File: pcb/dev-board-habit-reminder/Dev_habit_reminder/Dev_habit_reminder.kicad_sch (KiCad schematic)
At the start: 10 parts, among them J1 I2C BREAKOUT, SW1 SW_Push, SW2 SW_Push, SW3 SW_Push, U1 ESP32-DevKitC

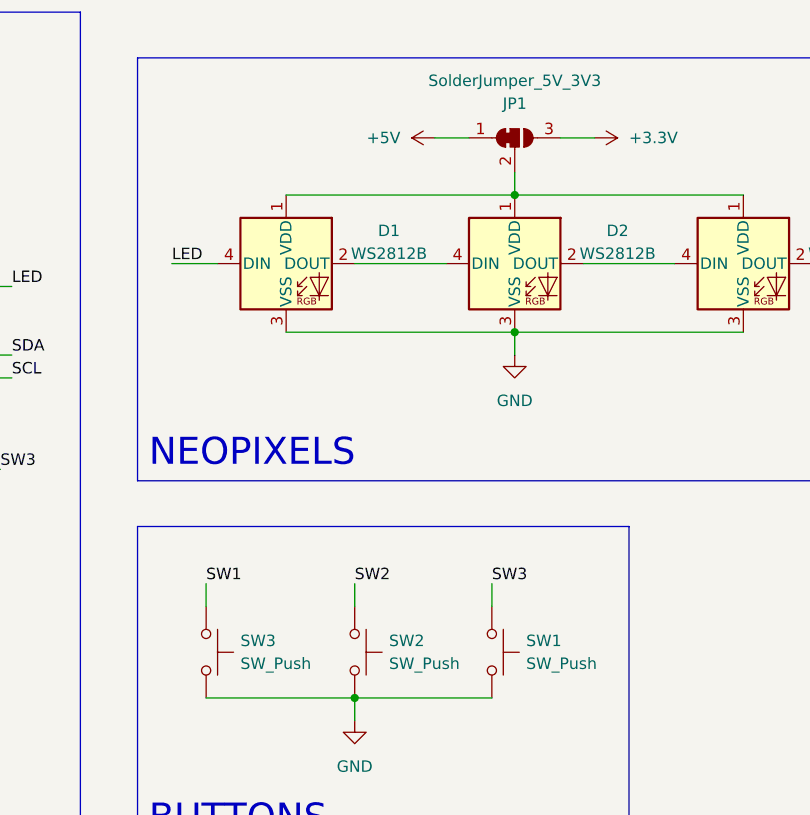
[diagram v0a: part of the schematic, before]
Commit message: PCB Track width definition, rerouting
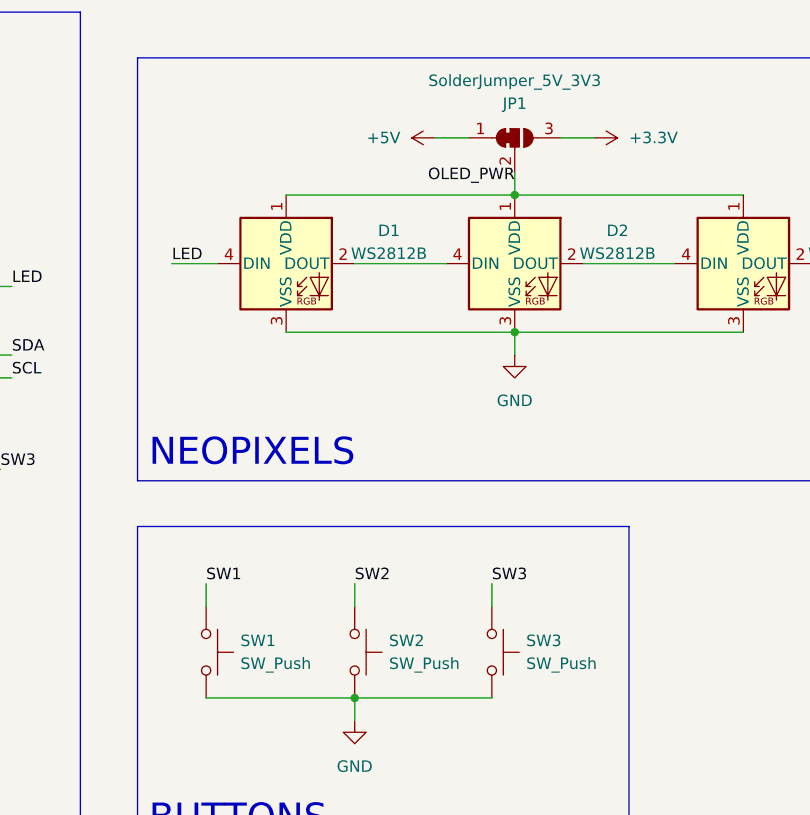
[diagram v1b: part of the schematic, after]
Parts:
- renumbered SW3 to SW1, SW1 to SW3
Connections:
- net OLED_PWR: now reaches D1.1 (VDD), D2.1 (VDD), D3.1 (VDD), JP1.2 (C)
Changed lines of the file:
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@@
     (effects (font (size 1.27 1.27)) (justify left bottom))
+  )
+  (label "OLED_PWR" (at 224.79 59.69 180) (fields_autoplaced)
+    (effects (font (size 1.27 1.27)) (justify right bottom))
   )
   (label "SW2" (at 207.01 104.14 0) (fields_autoplaced)
@@
   (label "SCL" (at 168.91 81.28 0) (fields_autoplaced)
     (effects (font (size 1.27 1.27)) (justify left bottom))
+  )
+  (netclass_flag "" (length 2.54) (shape round) (at 234.95 68.58 180) (fields_autoplaced)
+    (effects (font (size 1.27 1.27)) (justify right bottom))
+    (property "Netclass" "Signal" (at 235.6485 71.12 0)
+      (effects (font (size 1.27 1.27) italic) (justify left) hide)
+    )
+  )
+  (netclass_flag "" (length 2.54) (shape round) (at 210.82 68.58 180) (fields_autoplaced)
+    (effects (font (size 1.27 1.27)) (justify right bottom))
+    (property "Netclass" "Signal" (at 211.5185 71.12 0)
+      (effects (font (size 1.27 1.27) italic) (justify left) hide)
+    )
   )
   (symbol (lib_id "power:GND") (at 60.96 125.73 270) (unit 1)
@@
   (symbol (lib_id "Switch:SW_Push") (at 190.5 111.76 270) (unit 1)
     (in_bom yes) (on_board yes) (dnp no) (fields_autoplaced)
-    (property "Reference" "SW3" (at 194.31 110.49 90)
+    (property "Reference" "SW1" (at 194.31 110.49 90)
       (effects (font (size 1.27 1.27)) (justify left))
     )
@@
       (project "Dev_habit_reminder"
         (path "/00a14bb3-c2ab-4ff5-bcca-f0dba2d9bd5e"
-          (reference "SW3") (unit 1)
+          (reference "SW1") (unit 1)
         )
       )
@@
   (symbol (lib_id "Switch:SW_Push") (at 222.25 111.76 270) (unit 1)
     (in_bom yes) (on_board yes) (dnp no) (fields_autoplaced)
-    (property "Reference" "SW1" (at 226.06 110.49 90)
+    (property "Reference" "SW3" (at 226.06 110.49 90)
       (effects (font (size 1.27 1.27)) (justify left))
     )
@@
       (project "Dev_habit_reminder"
         (path "/00a14bb3-c2ab-4ff5-bcca-f0dba2d9bd5e"
-          (reference "SW1") (unit 1)
+          (reference "SW3") (unit 1)
         )
       )

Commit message: Board re-routing
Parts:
- D1, D3: MPN (none) -> C2843785
- SW1, SW2, SW3: MPN (none) -> C410366
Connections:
- net OLED_PWR renamed NEOPIXEL_PWR
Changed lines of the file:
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@@
     (effects (font (size 1.27 1.27)) (justify left bottom))
   )
-  (label "OLED_PWR" (at 224.79 59.69 180) (fields_autoplaced)
+  (label "NEOPIXEL_PWR" (at 224.79 59.69 180) (fields_autoplaced)
     (effects (font (size 1.27 1.27)) (justify right bottom))
   )
@@
       (effects (font (size 1.27 1.27)) hide)
     )
+    (property "MPN" "C410366" (at 190.5 111.76 90)
+      (effects (font (size 1.27 1.27)) hide)
+    )
     (pin "1")
     (pin "2")
@@
     )
     (property "Datasheet" "~" (at 227.33 111.76 0)
+      (effects (font (size 1.27 1.27)) hide)
+    )
+    (property "MPN" "C410366" (at 222.25 111.76 90)
       (effects (font (size 1.27 1.27)) hide)
     )
@@
     (property "Datasheet" "https://cdn-shop.adafruit.com/datasheets/WS2812B.pdf" (at 252.73 78.105 0)
       (effects (font (size 1.27 1.27)) (justify left top) hide)
+    )
+    (property "MPN" "C2843785" (at 250.19 68.58 0)
+      (effects (font (size 1.27 1.27)) hide)
     )
     (pin "1")
@@
       (effects (font (size 1.27 1.27)) hide)
     )
+    (property "MPN" "C410366" (at 207.01 111.76 90)
+      (effects (font (size 1.27 1.27)) hide)
+    )
     (pin "1")
     (pin "2")
@@
     )
   )
-  (symbol (lib_id "LED:WS2812B") (at 199.39 68.58 0) (unit 1)
+  (symbol (lib_name "WS2812B_1") (lib_id "LED:WS2812B") (at 199.39 68.58 0) (unit 1)
     (in_bom yes) (on_board yes) (dnp no) (fields_autoplaced)
     (property "Reference" "D1" (at 210.82 64.9321 0)
@@
       (effects (font (size 1.27 1.27)) (justify left top) hide)
     )
-    (pin "1")
+    (property "MPN" "C2843785" (at 199.39 68.58 0)
+      (effects (font (size 1.27 1.27)) hide)
+    )
+    (pin "1")

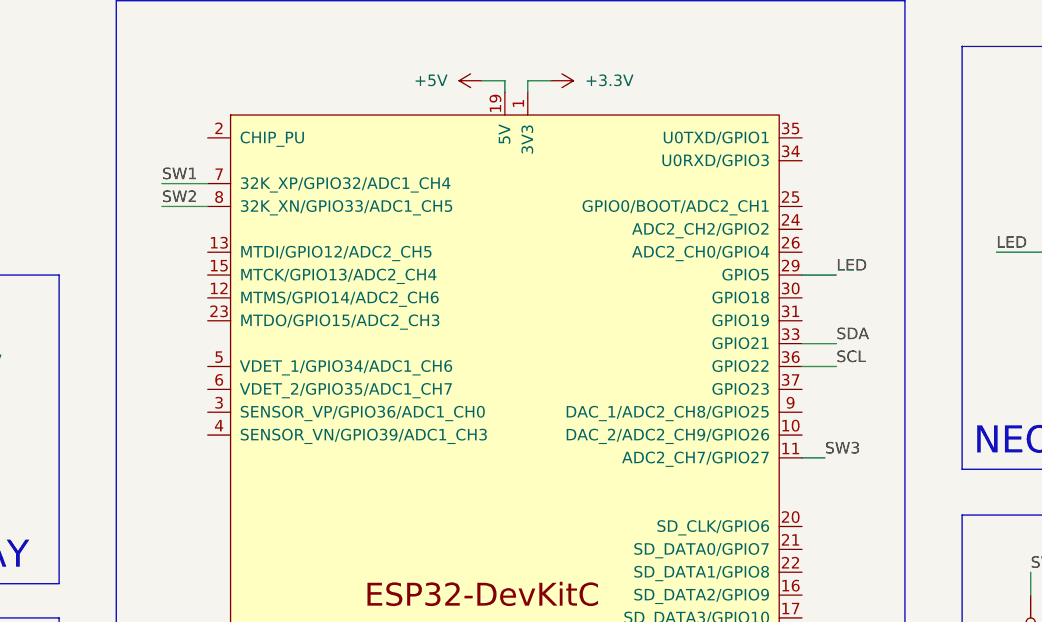
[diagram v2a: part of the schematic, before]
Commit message: Changed button pins for efficient routing
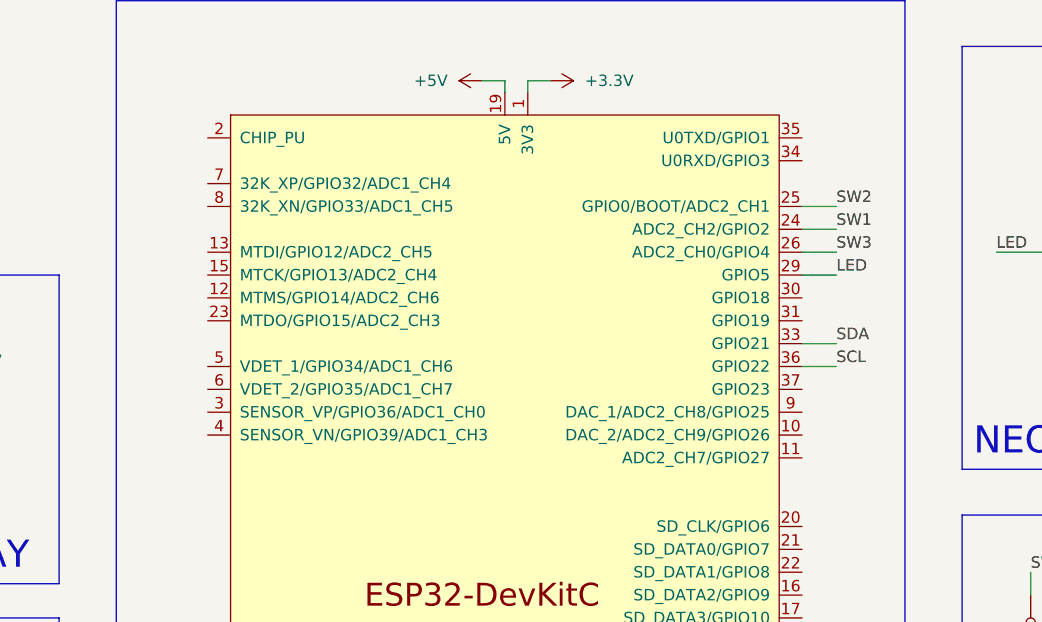
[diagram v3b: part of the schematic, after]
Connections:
- net SW1: now also U1.24 (ADC2_CH2/GPIO2); no longer U1.7 (32K_XP/GPIO32/ADC1_CH4)
- net SW2: now also U1.25 (GPIO0/BOOT/ADC2_CH1); no longer U1.8 (32K_XN/GPIO33/ADC1_CH5)
- net SW3: now also U1.26 (ADC2_CH0/GPIO4); no longer U1.11 (ADC2_CH7/GPIO27)
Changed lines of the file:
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@@
-    (stroke (width 0) (type default))
-  )
-  (wire (pts (xy 93.98 60.96) (xy 99.06 60.96))
     (stroke (width 0) (type default))
   )
@@
   )
   (wire (pts (xy 224.79 76.2) (xy 224.79 78.74))
+    (stroke (width 0) (type default))
+  )
+  (wire (pts (xy 165.1 66.04) (xy 168.91 66.04))
     (stroke (width 0) (type default))
   )
@@
   )
   (wire (pts (xy 233.68 54.61) (xy 229.87 54.61))
+    (stroke (width 0) (type default))
+  )
+  (wire (pts (xy 165.1 63.5) (xy 168.91 63.5))
     (stroke (width 0) (type default))
   )
@@
     (stroke (width 0) (type default))
   )
+  (wire (pts (xy 165.1 68.58) (xy 168.91 68.58))
+    (stroke (width 0) (type default))
+  )
   (wire (pts (xy 60.96 123.19) (xy 60.96 125.73))
     (stroke (width 0) (type default))
@@
     (stroke (width 0) (type default))
   )
-  (wire (pts (xy 93.98 63.5) (xy 99.06 63.5))
-    (stroke (width 0) (type default))
-  )
   (wire (pts (xy 207.01 104.14) (xy 207.01 106.68))
-    (stroke (width 0) (type default))
-  )
-  (wire (pts (xy 165.1 91.44) (xy 167.64 91.44))
     (stroke (width 0) (type default))
   )
@@
     (effects (font (size 1.27 1.27)) (justify left bottom))
   )
-  (label "SW2" (at 93.98 63.5 0) (fields_autoplaced)
-    (effects (font (size 1.27 1.27)) (justify left bottom))
-  )
   (label "SW3" (at 222.25 104.14 0) (fields_autoplaced)
     (effects (font (size 1.27 1.27)) (justify left bottom))
@@
     (effects (font (size 1.27 1.27)) (justify left bottom))
   )
+  (label "SW3" (at 168.91 68.58 0) (fields_autoplaced)
+    (effects (font (size 1.27 1.27)) (justify left bottom))
+  )
   (label "SW1" (at 190.5 104.14 0) (fields_autoplaced)
     (effects (font (size 1.27 1.27)) (justify left bottom))
   )
-  (label "SW1" (at 93.98 60.96 0) (fields_autoplaced)
-    (effects (font (size 1.27 1.27)) (justify left bottom))
-  )
-  (label "SW3" (at 167.64 91.44 0) (fields_autoplaced)
+  (label "SW2" (at 168.91 63.5 0) (fields_autoplaced)
     (effects (font (size 1.27 1.27)) (justify left bottom))
   )
@@
     (effects (font (size 1.27 1.27)) (justify left bottom))
   )
+  (label "SW1" (at 168.91 66.04 0) (fields_autoplaced)
+    (effects (font (size 1.27 1.27)) (justify left bottom))
+  )
